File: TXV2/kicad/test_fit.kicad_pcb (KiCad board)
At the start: 2 copper layers, 70 x 70 mm, 3 parts

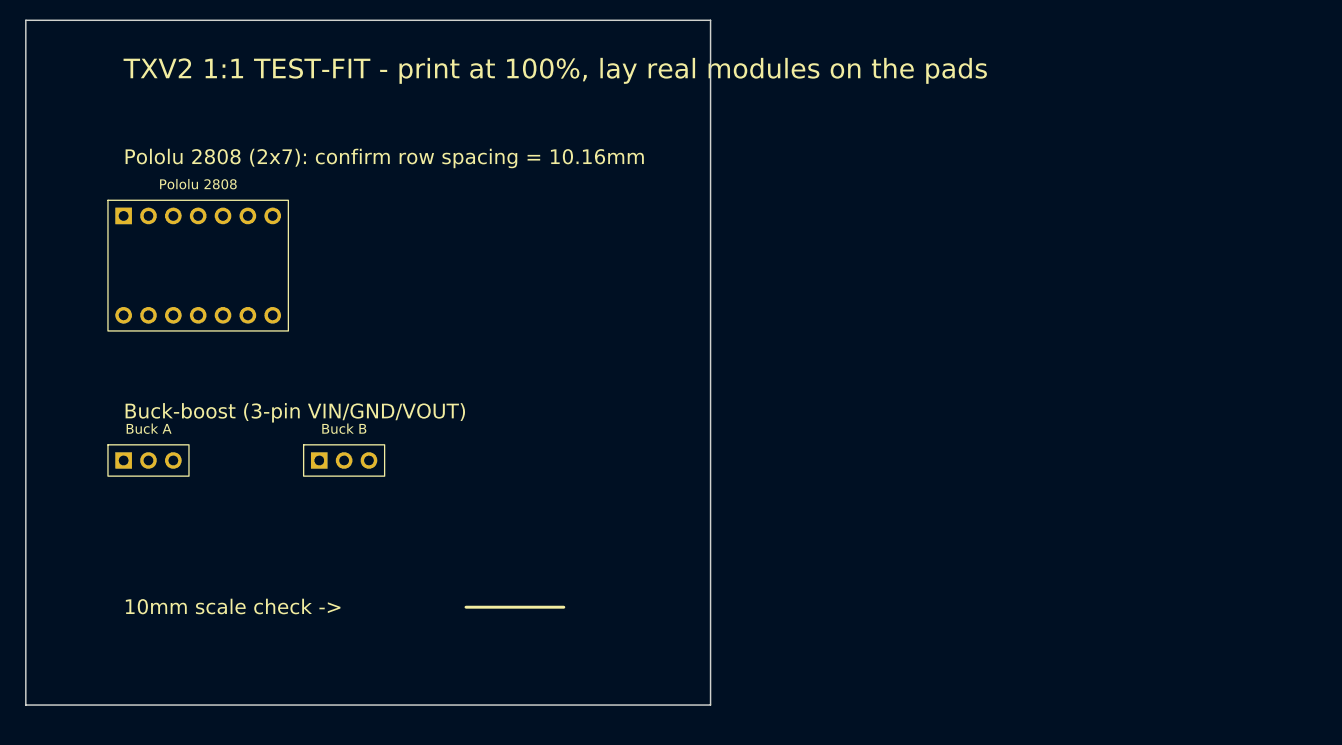
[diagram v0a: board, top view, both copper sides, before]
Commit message: TXV2 rev-A: correct Pololu 2808 (keyed 6+7, 12.3mm cols) + dual buck-boost split rail + soft-power button divider; placement 0 copper errors, routing in progress
Co-Authored-By: Claude Fable 5 <noreply@anthropic.com>
Claude-Session: https://claude.ai/code/session_01DvvNNevU4xtNTYtdVBAM7h
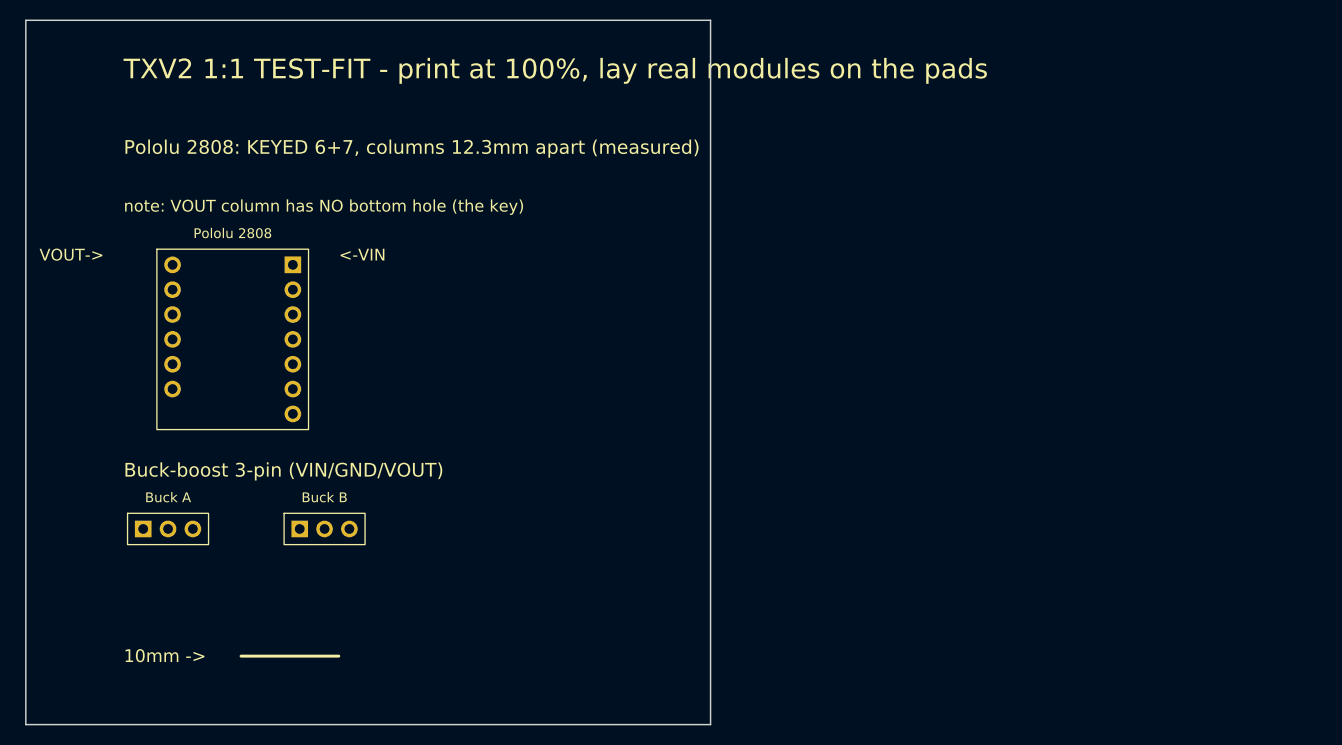
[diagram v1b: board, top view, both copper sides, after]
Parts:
- moved Buck A 7.28 mm to (42.0, 72.0)
- moved Buck B 7.28 mm to (58.0, 72.0)
- moved Pololu 2808 7.07 mm to (45.0, 45.0)
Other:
- board size 70 x 70 mm -> 70 x 72 mm
- board text added: "10mm ->"
- board text added: "<-VIN"
- board text added: "Buck-boost 3-pin (VIN/GND/VOUT)"
- board text added: "Pololu 2808: KEYED 6+7, columns 12.3mm apart (measured)"
- board text added: "VOUT->"
- board text added: "note: VOUT column has NO bottom hole (the key)"
- board text removed: "10mm scale check ->"
- board text removed: "Buck-boost (3-pin VIN/GND/VOUT)"
- board text removed: "Pololu 2808 (2x7): confirm row spacing = 10.16mm"
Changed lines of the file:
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@@
 	(general (thickness 1.6)) (paper "A4")
 	(layers (0 "F.Cu" signal) (2 "B.Cu" signal) (5 "F.SilkS" user) (1 "F.Mask" user) (25 "Edge.Cuts" user) (31 "F.CrtYd" user) (35 "F.Fab" user))
-	(setup)
-	(net 0 "")
+	(setup) (net 0 "")
 	(footprint "TXV2:Pololu2808_PSW03C"
 		(layer "F.Cu")
-		(at 40 40)
+		(at 45 45)
 		(attr through_hole)
-		(property "Reference" "Pololu 2808" (at 7.62 -3.2 0) (layer "F.SilkS") (effects (font (size 1 1) (thickness 0.15))))
-		(property "Value" "Pololu2808_PSW03C" (at 7.62 13.36 0) (layer "F.Fab") (effects (font (size 1 1) (thickness 0.15))))
+		(property "Reference" "Pololu 2808" (at 6.15 -3.2 0) (layer "F.SilkS") (effects (font (size 1 1) (thickness 0.15))))
+		(property "Value" "Pololu2808_PSW03C" (at 6.15 18.44 0) (layer "F.Fab") (effects (font (size 1 1) (thickness 0.15))))
 		(property "Footprint" "" (at 0 0 0) (layer "F.Fab") (hide yes) (effects (font (size 1.27 1.27))))
 		(property "Datasheet" "" (at 0 0 0) (layer "F.Fab") (hide yes) (effects (font (size 1.27 1.27))))
-		(property "Description" "Pololu 2808 PSW03C 2x7 - VERIFY ROW SPACING 10.16mm by paper test-fit" (at 0 0 0) (layer "F.Fab") (hide yes) (effects (font (size 1.27 1.27))))
-		(fp_rect (start -1.6 -1.6) (end 16.84 11.76) (stroke (width 0.12) (type solid)) (fill no) (layer "F.SilkS"))
-		(fp_rect (start -1.85 -1.85) (end 17.09 12.01) (stroke (width 0.05) (type solid)) (fill no) (layer "F.CrtYd"))
-		(pad "1" thru_hole rect (at 0.0 0) (size 1.7 1.7) (drill 1.0) (layers "*.Cu" "*.Mask") (remove_unused_layers no))
-		(pad "2" thru_hole circle (at 2.54 0) (size 1.7 1.7) (drill 1.0) (layers "*.Cu" "*.Mask") (remove_unused_layers no))
-		(pad "3" thru_hole circle (at 5.08 0) (size 1.7 1.7) (drill 1.0) (layers "*.Cu" "*.Mask") (remove_unused_layers no))
-		(pad "4" thru_hole circle (at 7.62 0) (size 1.7 1.7) (drill 1.0) (layers "*.Cu" "*.Mask") (remove_unused_layers no))
-		(pad "5" thru_hole circle (at 10.16 0) (size 1.7 1.7) (drill 1.0) (layers "*.Cu" "*.Mask") (remove_unused_layers no))
-		(pad "6" thru_hole circle (at 12.7 0) (size 1.7 1.7) (drill 1.0) (layers "*.Cu" "*.Mask") (remove_unused_layers no))
-		(pad "7" thru_hole circle (at 15.24 0) (size 1.7 1.7) (drill 1.0) (layers "*.Cu" "*.Mask") (remove_unused_layers no))
-		(pad "8" thru_hole circle (at 0.0 10.16) (size 1.7 1.7) (drill 1.0) (layers "*.Cu" "*.Mask") (remove_unused_layers no))
-		(pad "9" thru_hole circle (at 2.54 10.16) (size 1.7 1.7) (drill 1.0) (layers "*.Cu" "*.Mask") (remove_unused_layers no))
-		(pad "10" thru_hole circle (at 5.08 10.16) (size 1.7 1.7) (drill 1.0) (layers "*.Cu" "*.Mask") (remove_unused_layers no))
-		(pad "11" thru_hole circle (at 7.62 10.16) (size 1.7 1.7) (drill 1.0) (layers "*.Cu" "*.Mask") (remove_unused_layers no))
-		(pad "12" thru_hole circle (at 10.16 10.16) (size 1.7 1.7) (drill 1.0) (layers "*.Cu" "*.Mask") (remove_unused_layers no))
-		(pad "13" thru_hole circle (at 12.7 10.16) (size 1.7 1.7) (drill 1.0) (layers "*.Cu" "*.Mask") (remove_unused_layers no))
-		(pad "14" thru_hole circle (at 15.24 10.16) (size 1.7 1.7) (drill 1.0) (layers "*.Cu" "*.Mask") (remove_unused_layers no))
+		(property "Description" "Pololu 2808 PSW03C - KEYED 6+7 (no VOUT-col bottom hole), 12.3mm cols" (at 0 0 0) (layer "F.Fab") (hide yes) (effects (font (size 1.27 1.27))))
+		(fp_rect (start -1.6 -1.6) (end 13.9 16.84) (stroke (width 0.12) (type solid)) (fill no) (layer "F.SilkS"))
+		(fp_rect (start -1.85 -1.85) (end 14.15 17.09) (stroke (width 0.05) (type solid)) (fill no) (layer "F.CrtYd"))
+		(pad "1" thru_hole rect (at 12.3 0) (size 1.7 1.7) (drill 1.0) (layers "*.Cu" "*.Mask") (remove_unused_layers no))
+		(pad "2" thru_hole circle (at 12.3 2.54) (size 1.7 1.7) (drill 1.0) (layers "*.Cu" "*.Mask") (remove_unused_layers no))
+		(pad "3" thru_hole circle (at 12.3 5.08) (size 1.7 1.7) (drill 1.0) (layers "*.Cu" "*.Mask") (remove_unused_layers no))
+		(pad "4" thru_hole circle (at 12.3 7.62) (size 1.7 1.7) (drill 1.0) (layers "*.Cu" "*.Mask") (remove_unused_layers no))
+		(pad "5" thru_hole circle (at 12.3 10.16) (size 1.7 1.7) (drill 1.0) (layers "*.Cu" "*.Mask") (remove_unused_layers no))
+		(pad "6" thru_hole circle (at 12.3 12.7) (size 1.7 1.7) (drill 1.0) (layers "*.Cu" "*.Mask") (remove_unused_layers no))
+		(pad "7" thru_hole circle (at 12.3 15.24) (size 1.7 1.7) (drill 1.0) (layers "*.Cu" "*.Mask") (remove_unused_layers no))
+		(pad "8" thru_hole circle (at 0 0) (size 1.7 1.7) (drill 1.0) (layers "*.Cu" "*.Mask") (remove_unused_layers no))
+		(pad "9" thru_hole circle (at 0 2.54) (size 1.7 1.7) (drill 1.0) (layers "*.Cu" "*.Mask") (remove_unused_layers no))
+		(pad "10" thru_hole circle (at 0 5.08) (size 1.7 1.7) (drill 1.0) (layers "*.Cu" "*.Mask") (remove_unused_layers no))
+		(pad "11" thru_hole circle (at 0 7.62) (size 1.7 1.7) (drill 1.0) (layers "*.Cu" "*.Mask") (remove_unused_layers no))
+		(pad "12" thru_hole circle (at 0 10.16) (size 1.7 1.7) (drill 1.0) (layers "*.Cu" "*.Mask") (remove_unused_layers no))
+		(pad "13" thru_hole circle (at 0 12.7) (size 1.7 1.7) (drill 1.0) (layers "*.Cu" "*.Mask") (remove_unused_layers no))
 	)
 		(footprint "TXV2:Buck3pin_VGV"
 		(layer "F.Cu")
-		(at 40 65)
+		(at 42 72)
 		(attr through_hole)
 		(property "Reference" "Buck A" (at 2.54 -3.2 0) (layer "F.SilkS") (effects (font (size 1 1) (thickness 0.15))))
@@
 		(footprint "TXV2:Buck3pin_VGV"
 		(layer "F.Cu")
-		(at 60 65)
+		(at 58 72)
 		(attr through_hole)
 		(property "Reference" "Buck B" (at 2.54 -3.2 0) (layer "F.SilkS") (effects (font (size 1 1) (thickness 0.15))))
@@
 	)
 		(gr_text "TXV2 1:1 TEST-FIT - print at 100%, lay real modules on the pads" (at 40 25) (layer "F.SilkS") (effects (font (size 2 2) (thickness 0.3)) (justify left)))
-		(gr_text "Pololu 2808 (2x7): confirm row spacing = 10.16mm" (at 40 34) (layer "F.SilkS") (effects (font (size 1.5 1.5) (thickness 0.25)) (justify left)))
-		(gr_text "Buck-boost (3-pin VIN/GND/VOUT)" (at 40 60) (layer "F.SilkS") (effects (font (size 1.5 1.5) (thickness 0.25)) (justify left)))
-		(gr_text "10mm scale check ->" (at 40 80) (layer "F.SilkS") (effects (font (size 1.5 1.5) (thickness 0.25)) (justify left)))
-		(gr_line (start 75 80) (end 85 80) (stroke (width 0.3) (type solid)) (layer "F.SilkS"))
-		(gr_rect (start 30 20) (end 100 90) (stroke (width 0.15) (type solid)) (fill no) (layer "Edge.Cuts"))
+		(gr_text "Pololu 2808: KEYED 6+7, columns 12.3mm apart (measured)" (at 40 33) (layer "F.SilkS") (effects (font (size 1.4 1.4) (thickness 0.22)) (justify left)))
+		(gr_text "note: VOUT column has NO bottom hole (the key)" (at 40 39) (layer "F.SilkS") (effects (font (size 1.2 1.2) (thickness 0.2)) (justify left)))
+		(gr_text "VOUT->" (at 38 44) (layer "F.SilkS") (effects (font (size 1.2 1.2) (thickness 0.2)) (justify right)))
+		(gr_text "<-VIN" (at 62 44) (layer "F.SilkS") (effects (font (size 1.2 1.2) (thickness 0.2)) (justify left)))
+		(gr_text "Buck-boost 3-pin (VIN/GND/VOUT)" (at 40 66) (layer "F.SilkS") (effects (font (size 1.4 1.4) (thickness 0.22)) (justify left)))
+		(gr_text "10mm ->" (at 40 85) (layer "F.SilkS") (effects (font (size 1.3 1.3) (thickness 0.2)) (justify left)))
+		(gr_line (start 52 85) (end 62 85) (stroke (width 0.3) (type solid)) (layer "F.SilkS"))
+		(gr_rect (start 30 20) (end 100 92) (stroke (width 0.15) (type solid)) (fill no) (layer "Edge.Cuts"))
 )
